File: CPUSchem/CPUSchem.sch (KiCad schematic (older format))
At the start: 31 parts

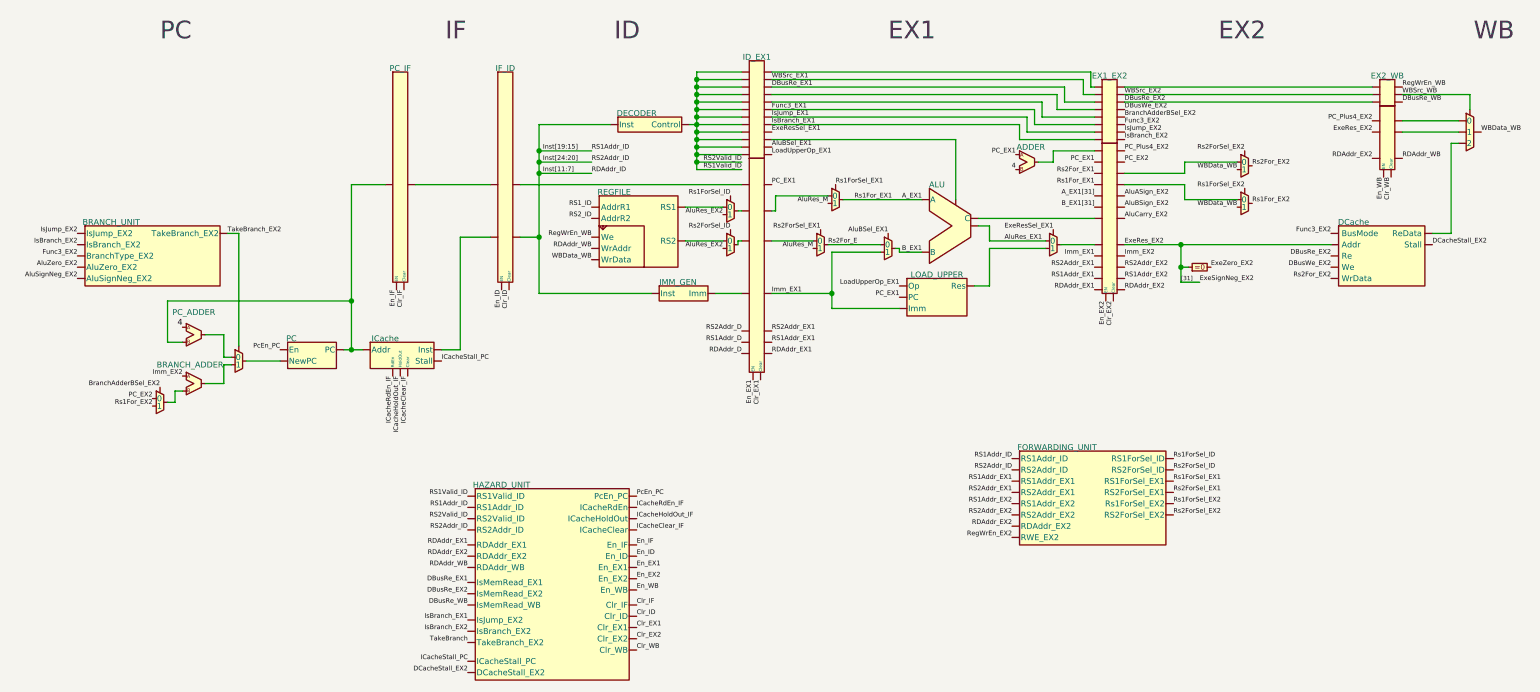
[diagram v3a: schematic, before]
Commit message: Updated CPU schematic
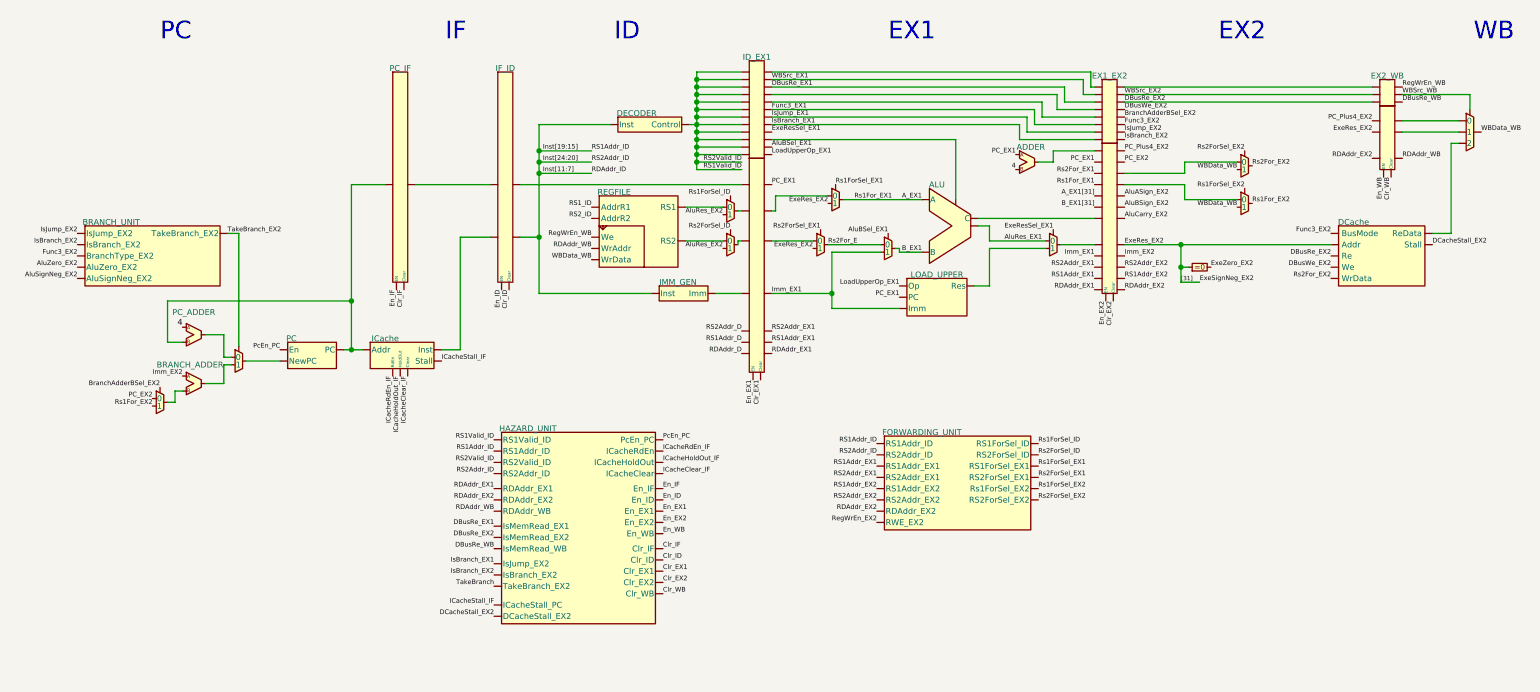
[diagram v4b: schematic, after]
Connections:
- net ExeRes_EX2: now also U?.~, U?.~
- net ICacheStall_IF: now reaches U?.~ (Stall)
- net ICacheStall_IF: now also U?.~ (TakeBranch_EX2); no longer U?.~
- removed net AluRes_M: U?.~, U?.~
- removed net ICacheStall_PC: U?.~ (Stall), U?.~ (TakeBranch_EX2)
- new net: U?.~, U?.~ (x21)
- new net: U?.~, U?.~ (Res)
- new net: U?.~, U?.~ (WrData) (x3)
- new net: U?.~, U?.~ (Inst)
- new net: U?.~, U?.~, U?.~ (PC), U?.~ (Stall)
- new net: U?.~, U?.~ (PC)
- new net: U?.~, U?.~ (Stall)
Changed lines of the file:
@@
 Text Label 5825 3025 0    31   ~ 0
 RS2Addr_EX1
-Text Label 7425 4100 2    31   ~ 0
+Text Label 6525 4000 2    31   ~ 0
 RS2Addr_EX1
 Text Label 5825 3175 0    31   ~ 0
@@
 Wire Wire Line
 	5325 1700 5325 1650
-Text Label 7425 4325 2    31   ~ 0
+Text Label 6525 4225 2    31   ~ 0
 RDAddr_EX2
 Wire Wire Line
@@
 Text Label 5625 1900 2    31   ~ 0
 RS2Valid_ID
-Text Label 7425 4400 2    31   ~ 0
+Text Label 6525 4300 2    31   ~ 0
 RegWrEn_EX2
 Text Label 5825 1550 0    31   ~ 0
@@
 $EndComp
 Text Label 6100 2475 2    31   ~ 0
-AluRes_M
+ExeRes_EX2
 Wire Wire Line
 	5825 2425 6100 2425
@@
 Wire Wire Line
 	4275 1975 4275 2400
-Text Label 4925 4125 0    31   ~ 0
+Text Label 5100 3750 0    31   ~ 0
 PcEn_PC
-Text Label 3800 4200 2    31   ~ 0
+Text Label 3975 3825 2    31   ~ 0
 RS1Addr_ID
-Text Label 3800 4350 2    31   ~ 0
+Text Label 3975 3975 2    31   ~ 0
 RS2Addr_ID
-Text Label 3800 4450 2    31   ~ 0
+Text Label 3975 4075 2    31   ~ 0
 RDAddr_EX1
-Text Label 3800 5025 2    31   ~ 0
+Text Label 3975 4650 2    31   ~ 0
 IsBranch_EX2
 $Comp
@@
 Text Label 2200 2375 0    31   ~ 0
 TakeBranch_EX2
-Text Label 3800 5100 2    31   ~ 0
+Text Label 3975 4725 2    31   ~ 0
 TakeBranch
-Text Label 4925 4600 0    31   ~ 0
+Text Label 5100 4225 0    31   ~ 0
 En_EX1
-Text Label 4925 5000 0    31   ~ 0
+Text Label 5100 4625 0    31   ~ 0
 Clr_EX1
-Text Label 4925 4525 0    31   ~ 0
+Text Label 5100 4150 0    31   ~ 0
 En_ID
-Text Label 4925 4925 0    31   ~ 0
+Text Label 5100 4550 0    31   ~ 0
 Clr_ID
-Text Label 4925 4675 0    31   ~ 0
+Text Label 5100 4300 0    31   ~ 0
 En_EX2
-Text Label 4925 5075 0    31   ~ 0
+Text Label 5100 4700 0    31   ~ 0
 Clr_EX2
 Text Label 2550 3150 2    31   ~ 0
@@
 L CPUSchem:HAZARD_UNIT U?
 U 1 1 5EBA3150
-P 4200 4275
+P 4375 3900
 AR Path="/5EBA3150" Ref="U?"  Part="1"
 AR Path="/5EB97B98/5EBA3150" Ref="U?"  Part="1"
-F 0 "U?" H 4100 4650 31  0001 C CNN
-F 1 "HAZARD_UNIT" H 4025 4500 39  0000 C CNN
-F 2 "" H 4100 4650 31  0001 C CNN
-F 3 "" H 4100 4650 31  0001 C CNN
-	1    4200 4275
+F 0 "U?" H 4275 4275 31  0001 C CNN
+F 1 "HAZARD_UNIT" H 4200 4125 39  0000 C CNN
+F 2 "" H 4275 4275 31  0001 C CNN
+F 3 "" H 4275 4275 31  0001 C CNN
+	1    4375 3900
 	1    0    0    -1
 $EndComp
 Text Label 1200 2600 2    31   ~ 0
 AluZero_EX2
-Text Label 3800 4525 2    31   ~ 0
+Text Label 3975 4150 2    31   ~ 0
 RDAddr_EX2
 Wire Wire Line
 	3100 3150 3025 3150
-Text Label 4925 4200 0    31   ~ 0
+Text Label 5100 3825 0    31   ~ 0
 ICacheRdEn_IF
 $Comp
@@
 Text Label 1200 2675 2    31   ~ 0
 AluSignNeg_EX2
-Text Label 3800 4275 2    31   ~ 0
+Text Label 3975 3900 2    31   ~ 0
 RS2Valid_ID
-Text Label 3800 4125 2    31   ~ 0
+Text Label 3975 3750 2    31   ~ 0
 RS1Valid_ID
 Wire Wire Line
@@
 Text Label 4625 1975 0    31   ~ 0
 RDAddr_ID
-Text Label 8500 4025 0    31   ~ 0
+Text Label 7600 3925 0    31   ~ 0
 Rs1ForSel_EX1
 Text Label 4625 2200 2    31   ~ 0
@@
 Text Label 5825 1650 0    31   ~ 0
 IsBranch_EX1
-Text Label 3800 4700 2    31   ~ 0
+Text Label 3975 4325 2    31   ~ 0
 DBusRe_EX1
 Wire Wire Line
@@
 	5850 2125 6200 2125
 Text Label 6200 2175 2    31   ~ 0
-AluRes_M
+ExeRes_EX2
 Wire Wire Line
 	6225 2500 6225 2775
@@
 	1    0    0    -1
 $EndComp
-Text Label 8500 4100 0    31   ~ 0
+Text Label 7600 4000 0    31   ~ 0
 Rs2ForSel_EX1
-Text Label 8500 4175 0    31   ~ 0
+Text Label 7600 4075 0    31   ~ 0
 Rs1ForSel_EX2
 Text Label 6375 2150 0    31   ~ 0
@@
 Text Label 1700 3525 2    31   ~ 0
 Rs1For_EX2
-Text Label 7425 4175 2    31   ~ 0
+Text Label 6525 4075 2    31   ~ 0
 RS1Addr_EX2
 Text Label 4625 2400 2    31   ~ 0
@@
 	5325 1350 5325 1400
 Connection ~ 5325 1400
-Text Label 4925 5150 0    31   ~ 0
+Text Label 5100 4775 0    31   ~ 0
 Clr_WB
-Text Label 4925 4750 0    31   ~ 0
+Text Label 5100 4375 0    31   ~ 0
 En_WB
-Text Label 8500 4250 0    31   ~ 0
+Text Label 7600 4150 0    31   ~ 0
 Rs2ForSel_EX2
 Text Label 6250 2050 0    31   ~ 0
@@
 Text Label 5500 2475 2    31   ~ 0
 AluRes_EX2
-Text Label 7425 4025 2    31   ~ 0
+Text Label 6525 3925 2    31   ~ 0
 RS1Addr_EX1
-Text Label 7425 4250 2    31   ~ 0
+Text Label 6525 4150 2    31   ~ 0
 RS2Addr_EX2
-Text Label 7425 3875 2    31   ~ 0
+Text Label 6525 3775 2    31   ~ 0
 RS1Addr_ID
-Text Label 7425 3950 2    31   ~ 0
+Text Label 6525 3850 2    31   ~ 0
 RS2Addr_ID
 Text Label 6600 2375 2    31   ~ 0
@@
 	5325 1300 5325 1350
 Connection ~ 5325 1350
-Text Label 3800 4600 2    31   ~ 0
+Text Label 3975 4225 2    31   ~ 0
 RDAddr_WB
-Text Label 3800 4775 2    31   ~ 0
+Text Label 3975 4400 2    31   ~ 0
 DBusRe_EX2
-Text Label 3800 4850 2    31   ~ 0
+Text Label 3975 4475 2    31   ~ 0
 DBusRe_WB
 Text Label 5825 1800 0    31   ~ 0
@@
 Text Label 4075 2750 3    31   ~ 0
 Clr_ID
-Text Label 4925 4450 0    31   ~ 0
+Text Label 5100 4075 0    31   ~ 0
 En_IF
-Text Label 4925 4850 0    31   ~ 0
+Text Label 5100 4475 0    31   ~ 0
 Clr_IF
 Wire Wire Line
@@
 Text Label 6150 2350 2    31   ~ 0
 Rs2ForSel_EX1
-Text Label 3800 4950 2    31   ~ 0
+Text Label 3975 4575 2    31   ~ 0
 IsBranch_EX1
 Text Notes 6600 1100 0    118  ~ 0
@@
 Text Label 7975 2600 2    31   ~ 0
 RS2Addr_EX1
-Text Label 8500 3875 0    31   ~ 0
+Text Label 7600 3775 0    31   ~ 0
 Rs1ForSel_ID
 Text Label 7375 2425 0    31   ~ 0
@@
 L CPUSchem:FORWARDING_UNIT U?
 U 1 1 5EBA3206
-P 7775 3975
+P 6875 3875
 AR Path="/5EBA3206" Ref="U?"  Part="1"
 AR Path="/5EB97B98/5EBA3206" Ref="U?"  Part="1"
-F 0 "U?" H 7775 4250 31  0001 C CNN
-F 1 "FORWARDING_UNIT" H 7725 4150 39  0000 C CNN
-F 2 "" H 7775 3975 31  0001 C CNN
-F 3 "" H 7775 3975 31  0001 C CNN
-	1    7775 3975
+F 0 "U?" H 6875 4150 31  0001 C CNN
+F 1 "FORWARDING_UNIT" H 6825 4050 39  0000 C CNN
+F 2 "" H 6875 3875 31  0001 C CNN
+F 3 "" H 6875 3875 31  0001 C CNN
+	1    6875 3875
 	1    0    0    -1
 $EndComp
@@
 Wire Wire Line
 	1800 3100 1900 3100
-Text Label 8500 3950 0    31   ~ 0
+Text Label 7600 3850 0    31   ~ 0
 Rs2ForSel_ID
 Text Notes 10500 1100 0    118  ~ 0
@@
 	3025 2825 3025 3150
 Text Label 3625 3225 0    31   ~ 0
-ICacheStall_PC
+ICacheStall_IF
 Text Label 10225 2450 0    31   ~ 0
 DCacheStall_EX2
-Text Label 3800 5300 2    31   ~ 0
+Text Label 3975 4925 2    31   ~ 0
 DCacheStall_EX2
-Text Label 3800 5225 2    31   ~ 0
-ICacheStall_PC
+Text Label 3975 4850 2    31   ~ 0
+ICacheStall_IF
 Wire Wire Line
 	4275 1650 4750 1650
@@
 Text Label 8925 2200 2    31   ~ 0
 WBData_WB
-Text Label 4925 4275 0    31   ~ 0
+Text Label 5100 3900 0    31   ~ 0
 ICacheHoldOut_IF
-Text Label 4925 4350 0    31   ~ 0
+Text Label 5100 3975 0    31   ~ 0
 ICacheClear_IF
 Text Label 3400 3325 3    31   ~ 0
